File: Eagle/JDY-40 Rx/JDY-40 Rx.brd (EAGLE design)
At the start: 55.4 x 26.4 mm, 13 parts, among them IC1 LD117AV

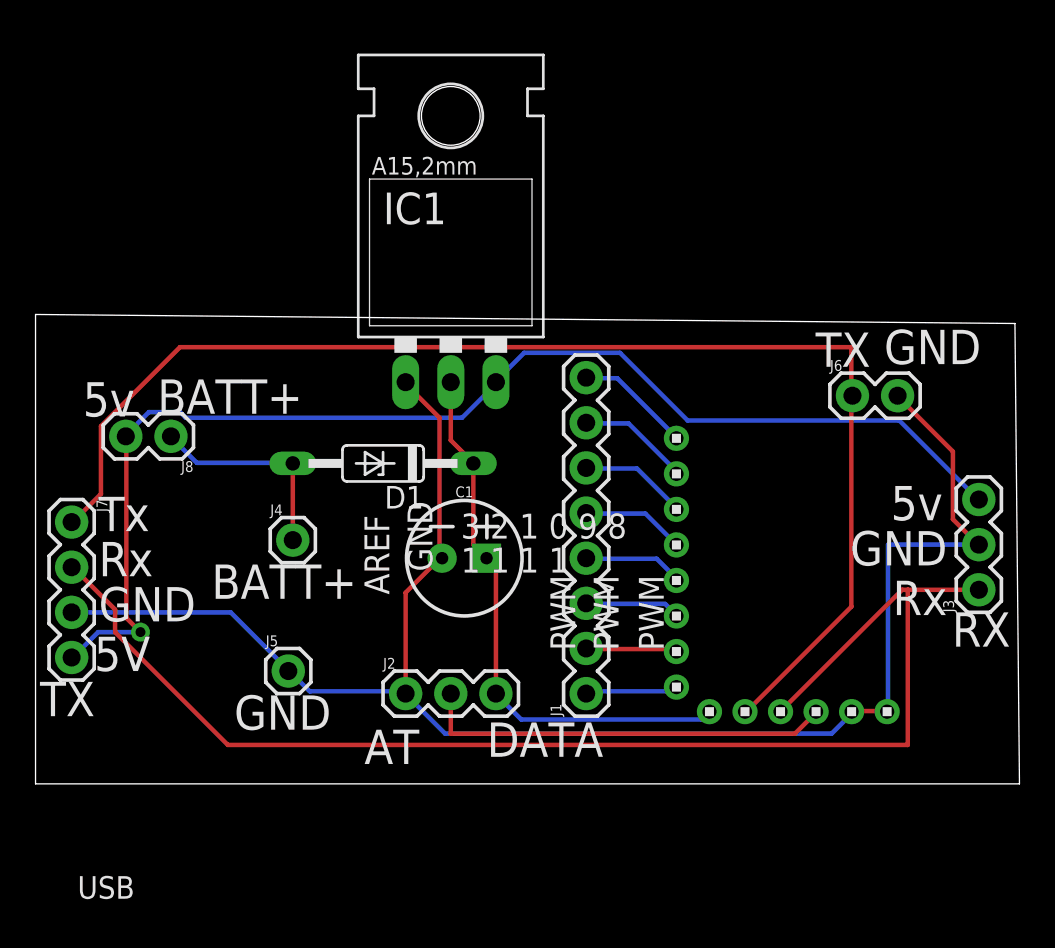
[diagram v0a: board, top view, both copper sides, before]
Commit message: Added Chrome App
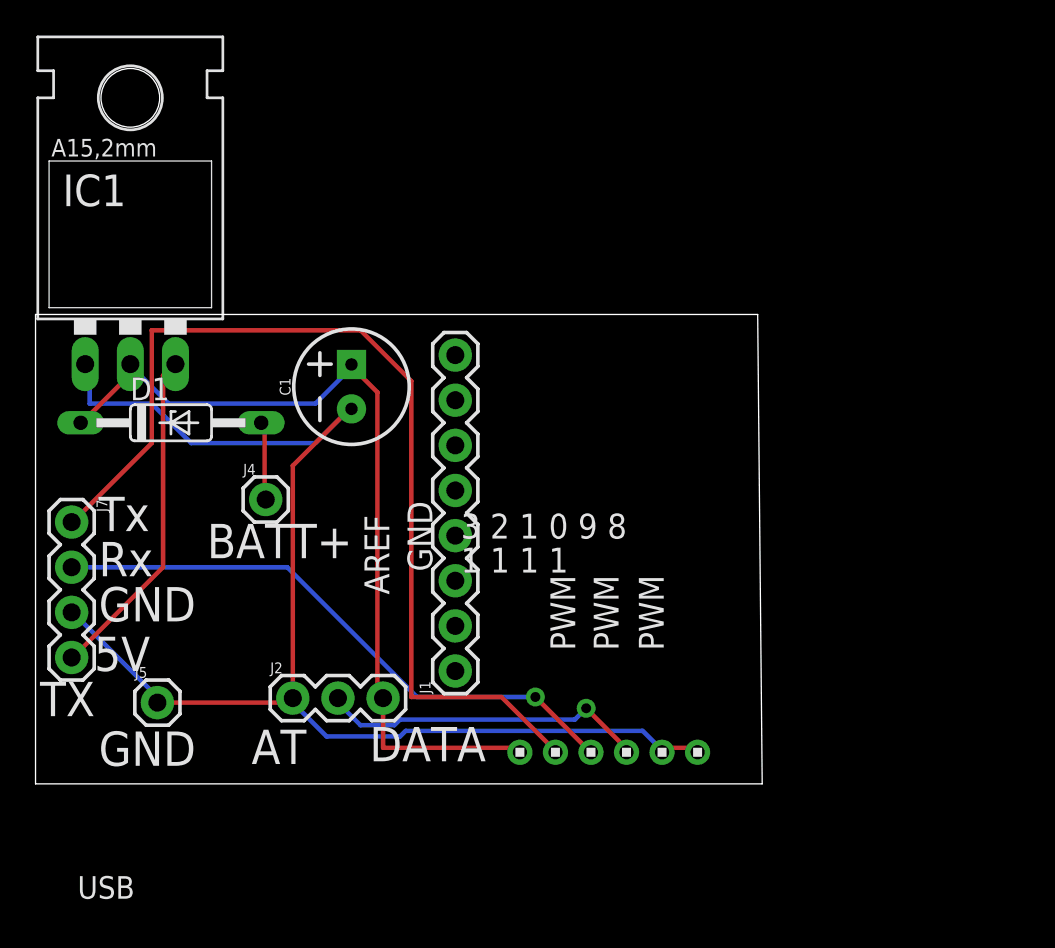
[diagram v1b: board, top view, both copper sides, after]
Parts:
- removed J3: (no value), SparkFun-Connectors:1X03
- removed J6, J8: (no value), SparkFun-Connectors:1X02
- removed U$2: 1X8, headers(2mm):1X8
- moved IC1 18.1 mm to (9.91, 61.0)
- moved D1 12.2 mm to (12.2, 53.8), turned to 0 degrees
- moved C1 11.6 mm to (22.4, 55.9), turned to 90 degrees
- moved U$1 10.9 mm to (36.8, 35.3)
- moved J5 7.58 mm to (11.4, 38.1)
- moved J1 7.47 mm to (28.2, 39.9)
- moved J2 6.36 mm to (19.1, 38.4)
- moved J4 2.75 mm to (17.5, 49.5)
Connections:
- removed net N$10: J1.6, U$2.6
- removed net N$11: J1.7, U$2.7
- removed net N$12: J1.8, U$2.8
- removed net N$5: J1.1, U$2.1
- removed net N$6: J1.2, U$2.2
- removed net N$7: J1.3, U$2.3
- removed net N$8: J1.4, U$2.4
- removed net N$9: J1.5, U$2.5
- net BATT+: no longer J8.1
- net GND_D: no longer J3.2, J6.2
- net RX_D: no longer J6.1
- net TX_D: no longer J3.1
- net VCC_D: no longer J3.3, J8.2
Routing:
- net VCC_D: track 69.6 -> 19.0 mm, vias 1 -> 0
- net TX_D: track 74.7 -> 33.5 mm, vias 0 -> 1
- net 3.3V_D: track 31.4 -> 49.2 mm
- net RX_D: track 73.3 -> 55.7 mm
- net GND_D: track 93.5 -> 76.4 mm
- net BATT+: track 11.8 -> 4.46 mm
- net N$12: track 6.54 -> 0.00 mm
- net N$11: track 6.37 -> 0.00 mm
- net N$10: track 6.11 -> 0.00 mm
- net N$9: track 5.85 -> 0.00 mm
- net N$8: track 5.68 -> 0.00 mm
- net N$7: track 5.42 -> 0.00 mm
- net N$5: track 5.35 -> 0.00 mm
- net N$6: track 5.25 -> 0.00 mm
- net SET: track 23.3 -> 18.5 mm, vias 0 -> 1
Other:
- board size 55.4 x 26.4 mm -> 40.9 x 26.4 mm
- board text removed: "5v"
- board text removed: "RX"

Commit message: eagle pcb-40 rx
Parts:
- added U$2, U$3, U$4, U$5, U$6, U$7, U$8, U$9: 1X1, headers(2mm):1X1
- moved U$1 1.78 mm to (38.6, 35.3)
- moved J1 1.55 mm to (28.4, 38.4)
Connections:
- new net N$1: J1.1, U$2.1
- new net N$2: J1.2, U$3.1
- new net N$3: J1.3, U$4.1
- new net N$4: J1.4, U$5.1
- new net N$5: J1.5, U$6.1
- new net N$6: J1.6, U$7.1
- new net N$7: J1.7, U$8.1
- new net N$8: J1.8, U$9.1
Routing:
- net TX_D: track 33.5 -> 67.2 mm
- net N$8: track 0.00 -> 5.16 mm
- net N$7: track 0.00 -> 4.90 mm
- net N$6: track 0.00 -> 4.77 mm
- net N$5: track 0.00 -> 4.44 mm
- net N$4: track 0.00 -> 4.31 mm
- net N$3: track 0.00 -> 3.99 mm
- net N$2: track 0.00 -> 3.85 mm
- net N$1: track 0.00 -> 3.71 mm
- net GND_D: track 76.4 -> 73.7 mm
- net SET: track 18.5 -> 21.2 mm
- net 3.3V_D: track 49.2 -> 51.5 mm
- net RX_D: track 55.7 -> 56.3 mm
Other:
- board size 40.9 x 26.4 mm -> 40.9 x 29 mm
